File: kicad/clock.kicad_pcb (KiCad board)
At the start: 4 copper layers, 110 x 110 mm, 186 parts, among them J1 USB4160-03-0230-C, J10 Knob: EM14 enc+SW (top face), J11 Radio-off toggle (rear), J12 NeoPixel ext (5V/DATA/GND, po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, J2 PROG, J3 Speaker DMA58-4 (4R), J6 DM3AT-SF-PEJM5, J7 Sensor board (BME688+TSL2591+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, J9 Wake COB 12V (warm+cool), M1 X40.879, Q1 2N7002, Q2 AO3401A, Q3 2N7002, Q4 AO3401A, Q6 AO3400A, Q7 AO3400A, Q8 2N7002, Q9 AO3401A, SW1 RESET, SW2 BOOT, U1 CH224K, U10 LTC4412ES6, U11 TB6612FNG, U12 TB6612FNG, U13 MCP23017, U14 QRE1113GR, U15 SN74AHCT1G125, U16 USBLC6-2SC6, U2 LT3652EMSE, U3 HY2111-GB, U4 AOSD32334C, U5 TPS61023, U6 TLV62569DBVR, U7 TPS55340PWPR, U8 ESP32-S3-WROOM-1-N16R8, U9 TAS5760MDAPR, Y1 32.768kHz

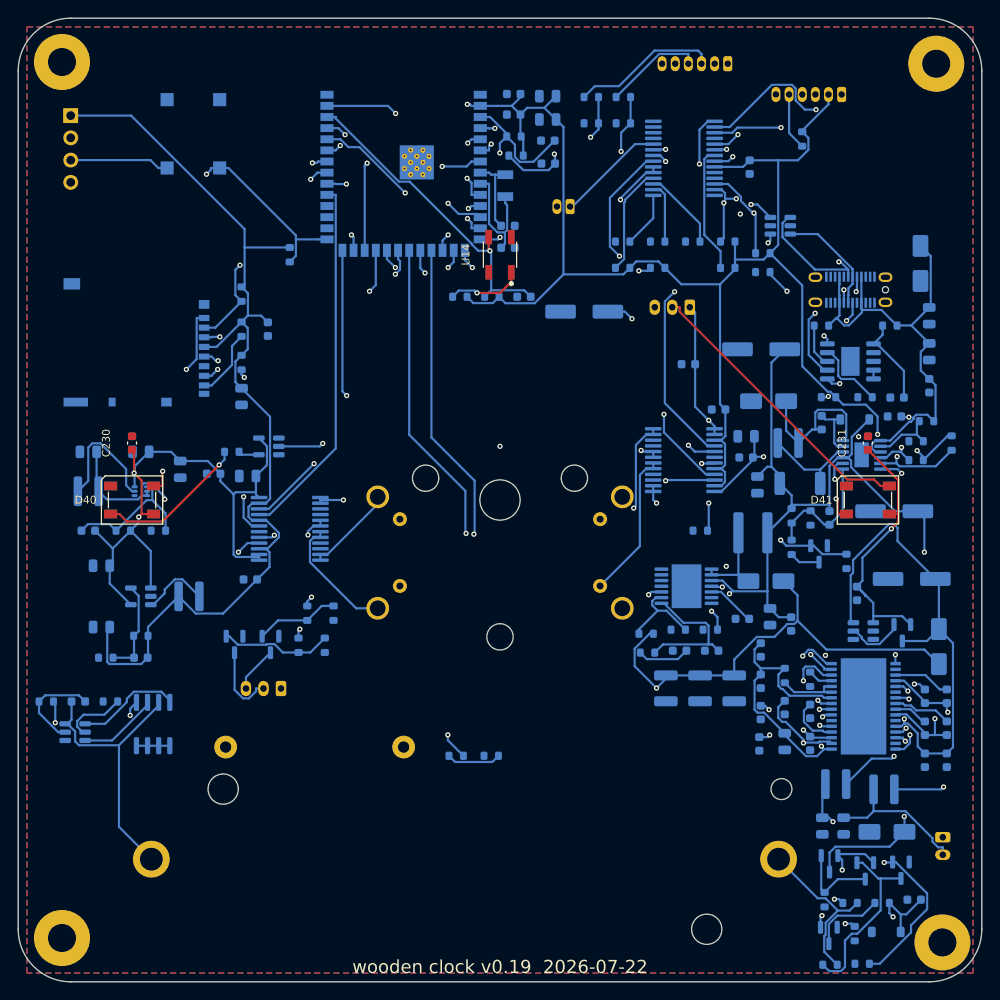
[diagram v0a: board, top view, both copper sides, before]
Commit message: kicad add routing and GND plane
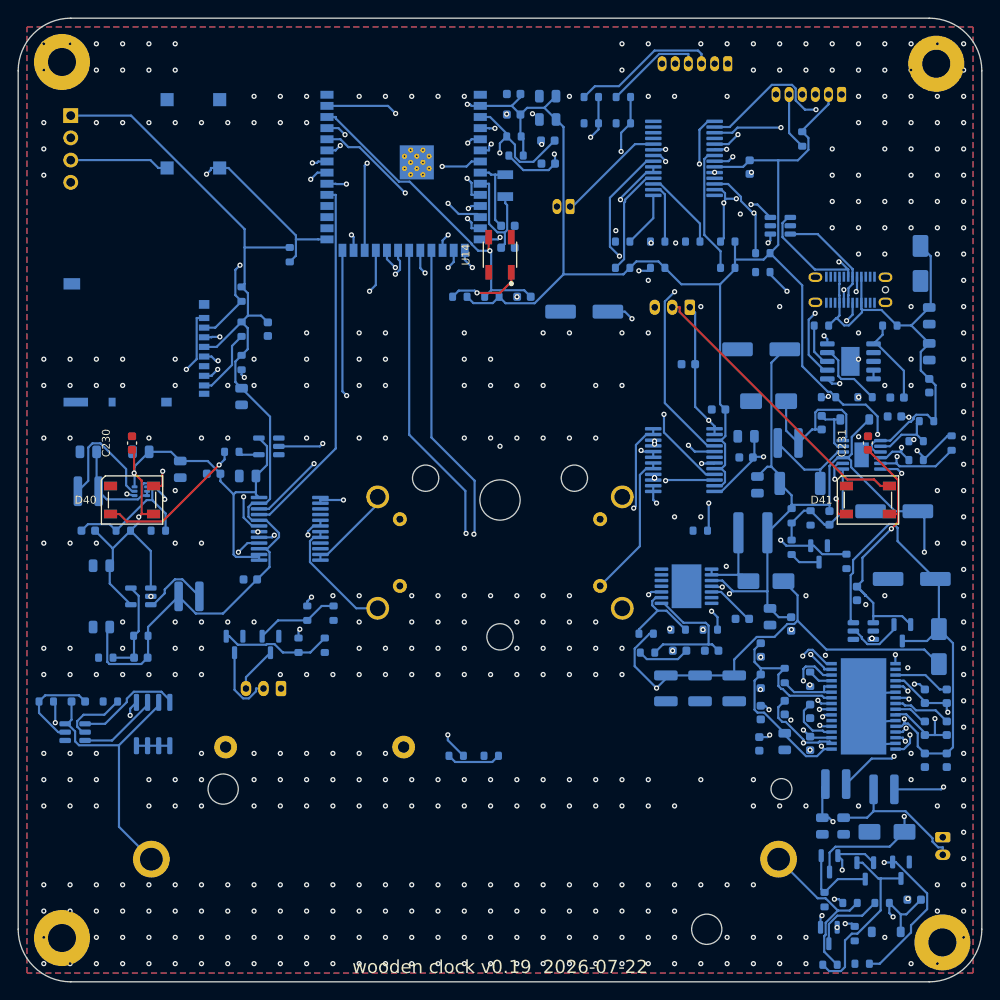
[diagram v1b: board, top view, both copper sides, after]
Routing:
- net GND: track 0.00 -> 12.5 mm, vias 0 -> 464

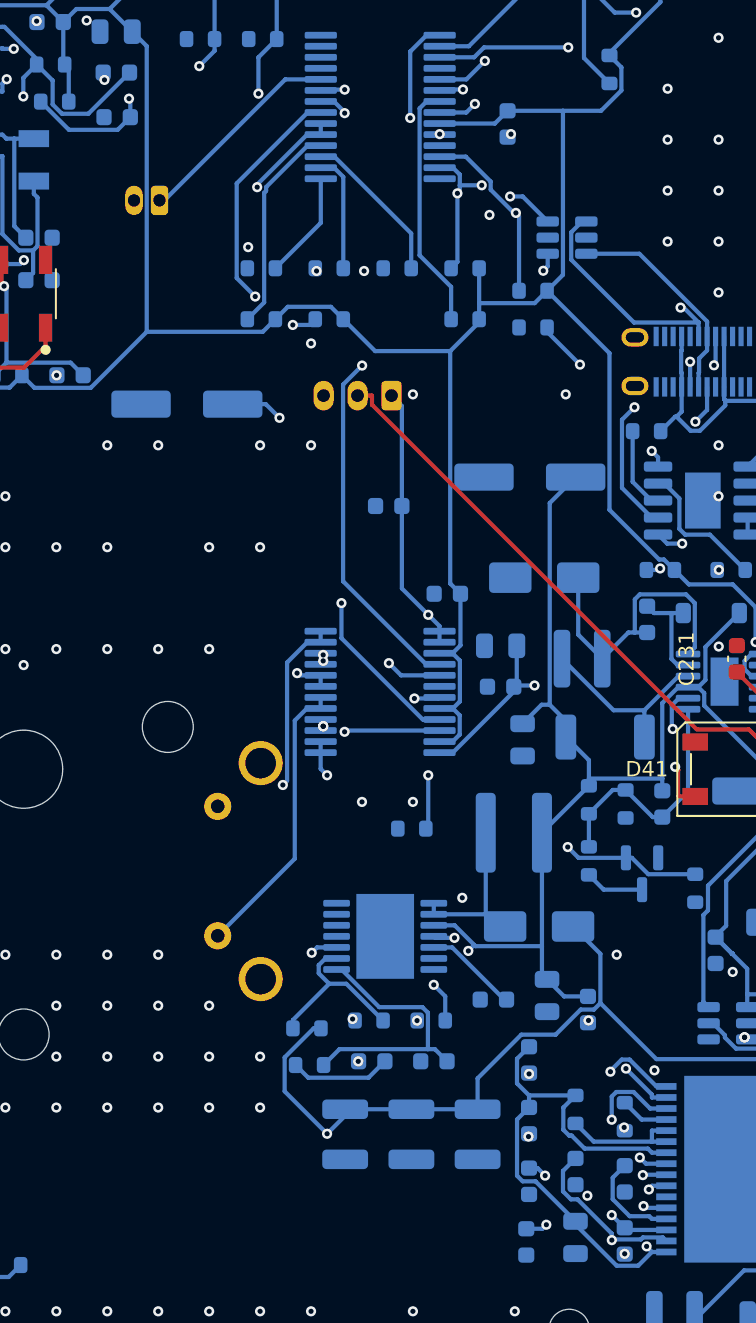
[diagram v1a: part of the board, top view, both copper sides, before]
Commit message: all connection except SPK_FAULT
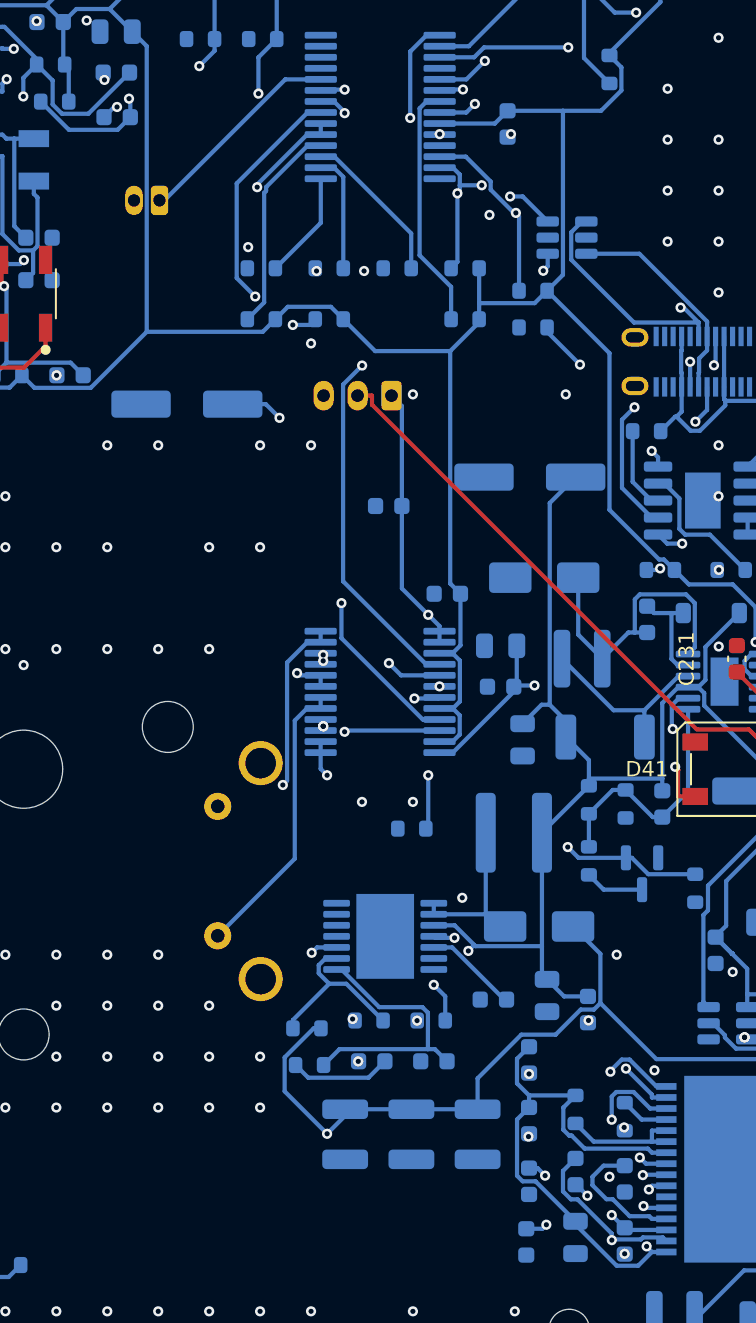
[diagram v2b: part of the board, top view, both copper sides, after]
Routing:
- net GND: track 12.5 -> 14.4 mm, vias 464 -> 467
- net Net-(U9-VCOM): track 5.91 -> 7.84 mm
- net I2C_SDA: track 133.2 -> 134.0 mm
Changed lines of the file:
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@@
 	)
 	(via
+		(at 79.4911 50.1224)
+		(size 0.6)
+		(drill 0.3)
+		(layers "F.Cu" "B.Cu")
+		(net "GND")
+	)
+	(via
 		(at 32.925 104.925)
 		(size 0.6)
@@
 	)
 	(via
+		(at 60.5 16)
+		(size 0.6)
+		(drill 0.3)
+		(layers "F.Cu" "B.Cu")
+		(free yes)
+		(net "GND")
+	)
+	(via
 		(at 2.925 5.925)
 		(size 0.6)
@@
 	)
 	(via
+		(at 89.5 79)
+		(size 0.6)
+		(drill 0.3)
+		(layers "F.Cu" "B.Cu")
+		(free yes)
+		(net "GND")
+	)
+	(via
 		(at 83.7 17.6005)
 		(size 0.6)
@@
 	)
 	(segment
+		(start 87.5 79.47)
+		(end 87.5511 79.47)
+		(width 0.25)
+		(layer "B.Cu")
+		(net "GND")
+	)
+	(segment
 		(start 13.2875 54.5)
 		(end 12.407167 54.312879)
@@
 	)
 	(segment
+		(start 60.3329 16)
+		(end 59.7329 16.6)
+		(width 0.25)
+		(layer "B.Cu")
+		(net "GND")
+	)
+	(segment
+		(start 87.5511 79.47)
+		(end 88.2 80.1189)
+		(width 0.25)
+		(layer "B.Cu")
+		(net "GND")
+	)
+	(segment
 		(start 100.15 80.182)
 		(end 96.508891 80.436611)
@@
 	)
 	(segment
+		(start 60.5 16)
+		(end 60.3329 16)
+		(width 0.25)
+		(layer "B.Cu")
+		(net "GND")
+	)
+	(segment
 		(start 101.675 48.2863)
 		(end 102.245633 48.100889)
@@
 	)
 	(segment
-		(start 87.25 8.0223)
-		(end 88.0173 7.255)
+		(start 80.5 51.5926)
+		(end 79.5926 52.5)
 		(width 0.25)
 		(layer "In1.Cu")
@@
 	)
 	(segment
-		(start 79.5926 22.0388)
-		(end 80.546 21.0854)
+		(start 87.25 8.0223)
+		(end 88.0173 7.255)
 		(width 0.25)
 		(layer "In1.Cu")
@@
 	)
 	(segment
-		(start 81.6209 13.6213)
-		(end 81.6209 13.0596)
+		(start 80.546 21.0854)
+		(end 79.5926 22.0388)
 		(width 0.25)
 		(layer "In1.Cu")
@@
 	)
 	(segment
-		(start 90.66 7.255)
-		(end 91 7.595)
+		(start 81.6209 13.6213)
+		(end 81.6209 13.0596)
 		(width 0.25)
 		(layer "In1.Cu")
@@
 	)
 	(segment
-		(start 79.5926 61.3343)
-		(end 79.5926 22.0388)
+		(start 90.66 7.255)
+		(end 91 7.595)
 		(width 0.25)
 		(layer "In1.Cu")
@@
 	)
 	(segment
-		(start 81.6209 13.0596)
-		(end 82.8617 11.8188)
+		(start 79.5926 22.0388)
+		(end 79.5926 49.0926)
 		(width 0.25)
 		(layer "In1.Cu")
@@
 	)
 	(segment
-		(start 80.8309 62.5726)
-		(end 79.5926 61.3343)
+		(start 81.6209 13.0596)
+		(end 82.8617 11.8188)
 		(width 0.25)
 		(layer "In1.Cu")
@@
 	)
 	(segment
+		(start 80.5 50)
+		(end 80.5 51.5926)
+		(width 0.25)
+		(layer "In1.Cu")
+		(net "I2C_SDA")
+	)
+	(segment
 		(start 81.9776 20.611)
 		(end 82.1116 20.477)
@@
 	)
 	(segment
+		(start 79.5926 49.0926)
+		(end 80.5 50)
+		(width 0.25)
+		(layer "In1.Cu")
+		(net "I2C_SDA")
+	)
+	(segment
 		(start 87.25 9.382)
 		(end 87.25 8.0223)
@@
 	)
 	(segment
+		(start 79.5926 52.5)
+		(end 79.5926 61.3343)
+		(width 0.25)
+		(layer "In1.Cu")
+		(net "I2C_SDA")
+	)
+	(segment
+		(start 79.5926 61.3343)
+		(end 80.8309 62.5726)
+		(width 0.25)
+		(layer "In1.Cu")
+		(net "I2C_SDA")
+	)
+	(segment
 		(start 84.8132 11.8188)
 		(end 87.25 9.382)
@@
 	)
 	(segment
-		(start 58.4313 18.2835)
-		(end 61.2057 15.5091)
+		(start 59.2165 18.2835)
+		(end 51.2395 18.2835)
+		(width 0.25)
+		(layer "In2.Cu")
+		(net "ENC_SW")
+	)
+	(segment
+		(start 61.2057 15.5091)
+		(end 61.2057 16.2943)
 		(width 0.25)
 		(layer "In2.Cu")
@@
 	)
 	(segment
-		(start 51.2395 18.2835)
-		(end 58.4313 18.2835)
+		(start 61.2057 16.2943)
+		(end 59.2165 18.2835)
 		(width 0.25)
 		(layer "In2.Cu")
@@
 	)
 	(segment
-		(start 90.4 78.3476)
-		(end 89.69 79.0576)
+		(start 90.6904 81.3245)
+		(end 89.69 80.3241)
 		(width 0.25)
 		(layer "B.Cu")
@@
 	)
 	(segment
-		(start 89.69 79.0576)
-		(end 89.69 80.3241)
+		(start 89.69 80.3241)
+		(end 89.3241 80.3241)
 		(width 0.25)
 		(layer "B.Cu")
@@
 	)
 	(segment
-		(start 91.8425 81.3245)
-		(end 92 81.482)
+		(start 92 81.482)
+		(end 91.8425 81.3245)
+		(width 0.25)
+		(layer "B.Cu")
+		(net "Net-(U9-VCOM)")
+	)
+	(segment
+		(start 89.1524 78.3476)
+		(end 90.4 78.3476)
+		(width 0.25)
+		(layer "B.Cu")
+		(net "Net-(U9-VCOM)")
+	)
+	(segment
+		(start 88.5 79)
+		(end 89.1524 78.3476)
 		(width 0.25)
 		(layer "B.Cu")
@@
 	)
 	(segment
-		(start 89.69 80.3241)
+		(start 89.3241 80.3241)
+		(end 88.5 79.5)
+		(width 0.25)
+		(layer "B.Cu")
+		(net "Net-(U9-VCOM)")
+	)
+	(segment
+		(start 91.8425 81.3245)
 		(end 90.6904 81.3245)
 		(width 0.25)
@@
 	)
 	(segment
-		(start 90.6904 81.3245)
-		(end 91.8425 81.3245)
+		(start 88.5 79.5)
+		(end 88.5 79)
 		(width 0.25)
 		(layer "B.Cu")
@@
 	(segment
 		(start 91.5044 80.7253)
-		(end 89.7135 78.9344)
+		(end 90.7791 80)
+		(width 0.25)
+		(layer "In1.Cu")
+		(net "Net-(U9-ANA_REF)")
+	)
+	(segment
+		(start 89 79.9344)
+		(end 88 78.9344)
+		(width 0.25)
+		(layer "In1.Cu")
+		(net "Net-(U9-ANA_REF)")
+	)
+	(segment
+		(start 90.7791 80)
+		(end 89 80)
 		(width 0.25)
 		(layer "In1.Cu")
@@
 	)
 	(segment
-		(start 89.7135 78.9344)
+		(start 88 78.9344)
 		(end 85.7107 78.9344)
 		(width 0.25)
 		(layer "In1.Cu")
+		(net "Net-(U9-ANA_REF)")
+	)
+	(segment
+		(start 89 80)
+		(end 89 79.9344)
+		(width 0.25)
+		(layer "In1.Cu")

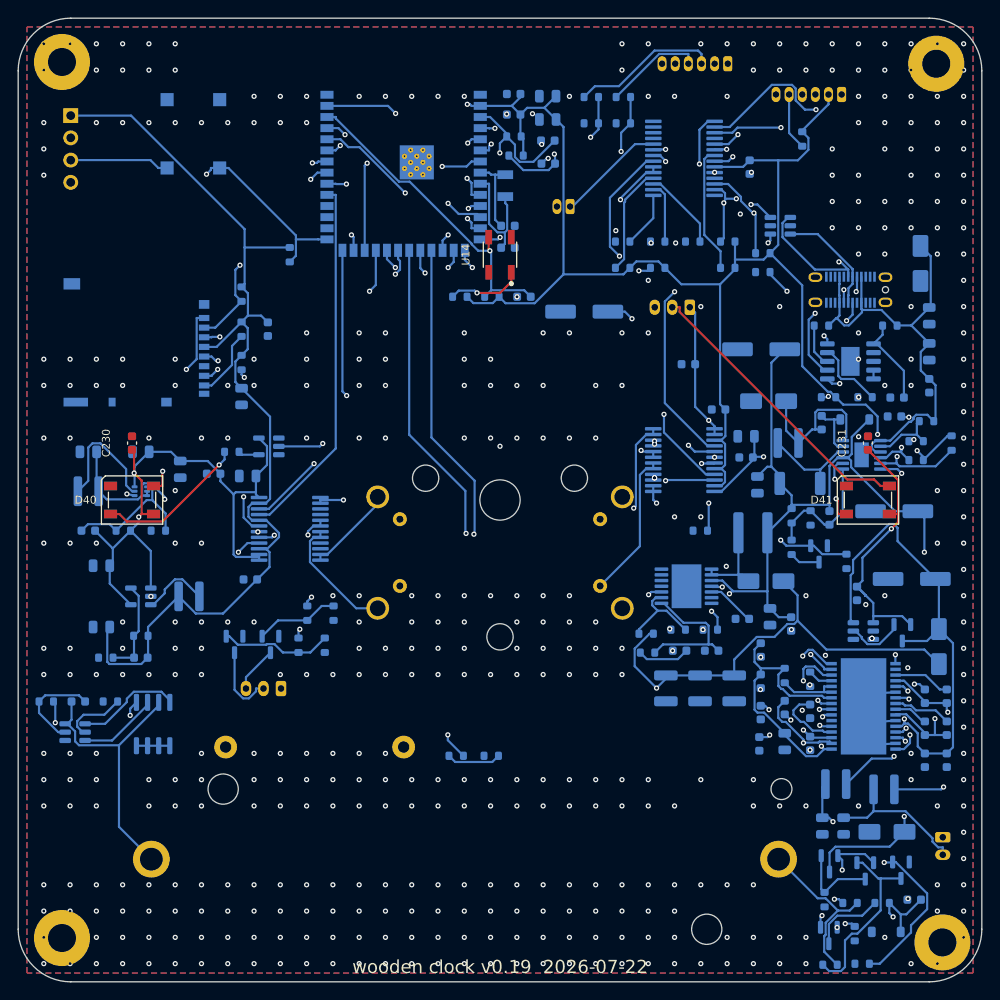
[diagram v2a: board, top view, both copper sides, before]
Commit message: fix all DRC issues manually
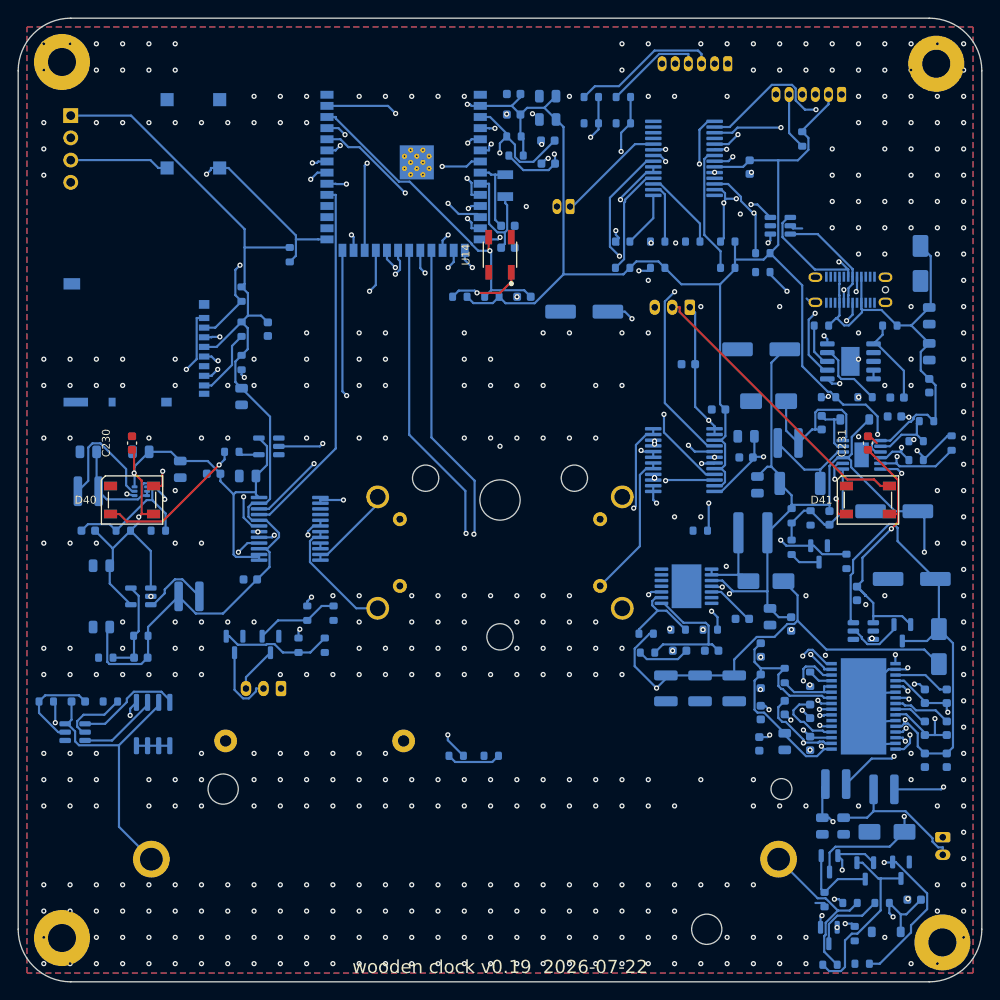
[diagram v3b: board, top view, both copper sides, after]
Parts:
- moved F1 0.70 mm to (44.0, 82.5)
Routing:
- net GND: track 14.4 -> 32.9 mm, vias 467 -> 468
- net SPK_SD: track 89.1 -> 89.6 mm

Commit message: manually fix all issues
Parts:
- moved C167 0.40 mm to (90.0, 79.1)
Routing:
- net SPK_FAULT: track 14.5 -> 76.0 mm, vias 0 -> 5
- net SPK_SD: track 89.6 -> 90.6 mm

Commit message: fix functional warnings
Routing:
- net GND: track 33.1 -> 35.7 mm, vias 468 -> 459
- net SPK_FAULT: track 76.0 -> 73.5 mm, vias 5 -> 4
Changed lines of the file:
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@@
 	)
 	(via
-		(at 5.925 5.925)
-		(size 0.6)
-		(drill 0.3)
-		(layers "F.Cu" "B.Cu")
-		(net "GND")
-	)
-	(via
 		(at 107.925 47.925)
 		(size 0.6)
@@
 	)
 	(via
-		(at 104.925 104.925)
-		(size 0.6)
-		(drill 0.3)
-		(layers "F.Cu" "B.Cu")
-		(net "GND")
-	)
-	(via
 		(at 44.925 86.925)
 		(size 0.6)
@@
 	)
 	(via
-		(at 97.4565 70.787761)
-		(size 0.6)
-		(drill 0.3)
-		(layers "F.Cu" "B.Cu")
-		(net "GND")
-	)
-	(via
 		(at 59.925 74.925)
 		(size 0.6)
@@
 	)
 	(via
-		(at 72.6411 52.469897)
-		(size 0.6)
-		(drill 0.3)
-		(layers "F.Cu" "B.Cu")
-		(net "GND")
-	)
-	(via
 		(at 77.925 86.925)
 		(size 0.6)
@@
 	)
 	(via
-		(at 104.925 5.925)
-		(size 0.6)
-		(drill 0.3)
-		(layers "F.Cu" "B.Cu")
-		(net "GND")
-	)
-	(via
 		(at 95.925 20.925)
 		(size 0.6)
@@
 	)
 	(via
-		(at 5.925 104.925)
-		(size 0.6)
-		(drill 0.3)
-		(layers "F.Cu" "B.Cu")
-		(net "GND")
-	)
-	(via
 		(at 65.925 41.925)
 		(size 0.6)
@@
 	)
 	(via
-		(at 72.6411 48.269897)
-		(size 0.6)
-		(drill 0.3)
-		(layers "F.Cu" "B.Cu")
-		(net "GND")
-	)
-	(via
 		(at 98.925 2.925)
 		(size 0.6)
@@
 	)
 	(via
-		(at 72.6411 52.469897)
-		(size 0.6)
-		(drill 0.3)
-		(layers "F.Cu" "B.Cu")
-		(net "GND")
-	)
-	(via
 		(at 23.925 68.925)
 		(size 0.6)
@@
 	)
 	(via
-		(at 97.4565 70.787761)
-		(size 0.6)
-		(drill 0.3)
-		(layers "F.Cu" "B.Cu")
-		(net "GND")
-	)
-	(via
 		(at 68.223 24.252835)
 		(size 0.6)
@@
 	)
 	(segment
+		(start 72.4911 52.7224)
+		(end 72.4911 52.0724)
+		(width 0.25)
+		(layer "B.Cu")
+		(net "GND")
+	)
+	(segment
 		(start 101.3676 74.332)
 		(end 101.55 74.1496)
@@
 	)
 	(segment
+		(start 97.6125 70.9106)
+		(end 98.0231 70.5)
+		(width 0.25)
+		(layer "B.Cu")
+		(net "GND")
+	)
+	(segment
 		(start 88.1375 23.6933)
 		(end 88.4442 24)
@@
 	)
 	(segment
+		(start 97.6125 70.9106)
+		(end 97.6125 69.9606)
+		(width 0.25)
+		(layer "B.Cu")
+		(net "GND")
+	)
+	(segment
 		(start 68.223 24.723)
 		(end 68.223 24.252835)
@@
 	)
 	(segment
+		(start 98.0231 70.5)
+		(end 98.5 70.5)
+		(width 0.25)
+		(layer "B.Cu")
+		(net "GND")
+	)
+	(segment
 		(start 101.675 48.2863)
 		(end 102.245633 48.100889)
@@
 	)
 	(via
-		(at 87 40)
-		(size 0.6)
-		(drill 0.3)
-		(layers "F.Cu" "B.Cu")
-		(net "SPK_FAULT")
-	)
-	(via
 		(at 80.175 28.5)
 		(size 0.6)
@@
 	)
 	(segment
-		(start 86 31)
-		(end 86 39)
-		(width 0.25)
-		(layer "In2.Cu")
-		(net "SPK_FAULT")
-	)
-	(segment
 		(start 93.0313 78.8327)
 		(end 93.0313 73.5)
@@
 	)
 	(segment
-		(start 83.5 28.5)
-		(end 80.175 28.5)
-		(width 0.25)
-		(layer "In2.Cu")
-		(net "SPK_FAULT")
-	)
-	(segment
-		(start 86 31.5)
-		(end 86 31)
-		(width 0.25)
-		(layer "In2.Cu")
-		(net "SPK_FAULT")
-	)
-	(segment
-		(start 86 31)
-		(end 83.5 28.5)
+		(start 80.175 33.175)
+		(end 87 40)
 		(width 0.25)
 		(layer "In2.Cu")
@@
 	)
 	(segment
-		(start 86 39)
-		(end 87 40)
+		(start 80.175 28.5)
+		(end 80.175 33.175)
 		(width 0.25)
 		(layer "In2.Cu")

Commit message: manually fix all warnings
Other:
- board text added: "Tibo - Wooden Clock v0.1"
- board text removed: "12V"
- board text removed: "3V3"
- board text removed: "5V"
- board text removed: "PROTECT"
- board text removed: "WAKE"
- board text removed: "clock v0.19"
- board text removed: "wooden clock v0.19 2026-07-22"
